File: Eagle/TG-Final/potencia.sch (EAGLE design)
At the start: 2 parts

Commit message: Schematic para Potencia
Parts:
- added D1: 15V, diode:ZENER-DIODEF126-10
- added IC1: 7812T, adafruit:7812T
- added JP2, JP3: (no value), SparkFun:M04LONGPADS
- added JP4: (no value), SparkFun:M06LONGPADS
- added LED1, LED2, LED3: (no value), adafruit:LED3MM
- added Q1: 2N3055, transistor-power:2N3055
- added R1, R3, R5: 1.8k, rcl:R-EU_0204/5
- added R10, R8, R9: 470, rcl:R-EU_0204/5
- added R11: 4.7K, rcl:R-EU_0204/5
- added R12: 1K, rcl:R-EU_0204/5
- added R2, R4, R6, R7: 1k, rcl:R-EU_0204/5
- added SG1: BUZZERPTH, SparkFun:BUZZERPTH
- added T1: 2N3904, transistor:2N3904
- added X1, X2, X3: (no value), con-wago-508:W237-2N
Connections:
- new net N$10: LED3.C, U$1.RB2/RX
- new net N$11: LED1.A, R8.2
- new net N$12: JP4.3, U$1.RB7/PGD
- new net N$13: LED2.A, R9.2
- new net N$14: LED3.A, R10.2
- new net N$15: JP4.2, U$1.RB6/PGC
- new net N$16: JP4.6, R7.2, U$1.RA5/MCLR
- new net N$17: R11.2, U$1.RB3
- new net N$18: X2-2.KL, X3-1.KL
- new net N$19: R11.1, T1.B
- new net N$2: R1.2, R2.1, U$1.RA0/AN0
- new net N$20: R12.1, SG1.1, T1.C
- new net N$21: D1.C, IC1.VI, X2-1.KL
- new net N$3: JP1.4, R3.1
- new net N$4: R3.2, R4.1, U$1.RA1/AN1
- new net N$5: JP2.4, R5.1
- new net N$6: R5.2, R6.1, U$1.RA2/AN2
- new net N$7: JP4.4, U$1.VSS
- new net N$8: LED1.C, U$1.RB0/INT
- new net N$9: LED2.C, U$1.RB1/SDA
- new net VDD: JP4.5, R10.1, R12.2, R7.1, R8.1, R9.1, SG1.2, U$1.VDD
- net N$1: now also JP3.4, R1.1; no longer JP1.2, U$1.RA4/AN4
- net VSS: now also D1.A, IC1.GND, JP2.1, JP3.1, R2.2, R4.2, R6.2, T1.E, X1-2.KL, X3-2.KL

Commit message: Esquematicos de Alimentación
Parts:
- added C1: 4700uf/25v, rcl:CPOL-USE10-30
- added C2, C3, C4: 0.1uf, rcl:C-EU050-024X044
- added C5: (no value), rcl:CPOL-USE2.5-6
- added D2: 1N4004, adafruit:1N4004
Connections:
- new net +12V: C4.1, C5.+, Q1.E
- new net N$22: C3.1, IC1.VO, Q1.B
- new net N$24: D2.A, IC1.GND
- net N$21: now also C1.+, C2.1, Q1.C
- net VSS: now also C1.-, C2.2, C3.2, C4.2, C5.-, D2.C; no longer IC1.GND
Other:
- moved on the sheet: D1, IC1, Q1
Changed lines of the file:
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@@
 <setting verticaltext="up"/>
 </settings>
-<grid distance="0.1" unitdist="inch" unit="inch" style="lines" multiple="1" display="no" altdistance="0.01" altunitdist="inch" altunit="inch"/>
+<grid distance="0.1" unitdist="inch" unit="inch" style="lines" multiple="1" display="yes" altdistance="0.01" altunitdist="inch" altunit="inch"/>
 <layers>
 <layer number="1" name="Top" color="4" fill="1" visible="no" active="no"/>
@@
 <part name="D1" library="diode" deviceset="ZENER-DIODE" device="F126-10" value="15V"/>
 <part name="VSS10" library="supply1" deviceset="VSS" device=""/>
+<part name="C1" library="rcl" deviceset="CPOL-US" device="E10-30" value="4700uf/25v"/>
+<part name="VSS12" library="supply1" deviceset="VSS" device=""/>
+<part name="C2" library="rcl" deviceset="C-EU" device="050-024X044" value="0.1uf"/>
 <part name="VSS11" library="supply1" deviceset="VSS" device=""/>
+<part name="D2" library="adafruit" deviceset="1N4004" device=""/>
+<part name="VSS13" library="supply1" deviceset="VSS" device=""/>
+<part name="C3" library="rcl" deviceset="C-EU" device="050-024X044" value="0.1uf"/>
+<part name="VSS14" library="supply1" deviceset="VSS" device=""/>
+<part name="C4" library="rcl" deviceset="C-EU" device="050-024X044" value="0.1uf"/>
+<part name="VSS15" library="supply1" deviceset="VSS" device=""/>
+<part name="C5" library="rcl" deviceset="CPOL-US" device="E2.5-6"/>
+<part name="VSS16" library="supply1" deviceset="VSS" device=""/>
+<part name="P+1" library="supply1" deviceset="+12V" device=""/>
 </parts>
 <sheets>
@@
 <instance part="X3" gate="-1" x="27.94" y="30.48"/>
 <instance part="X3" gate="-2" x="27.94" y="25.4"/>
-<instance part="VSS8" gate="G$1" x="35.56" y="20.32"/>
+<instance part="VSS8" gate="G$1" x="35.56" y="10.16"/>
 <instance part="VSS9" gate="G$1" x="35.56" y="66.04"/>
-<instance part="Q1" gate="A" x="116.84" y="35.56" rot="R90"/>
-<instance part="IC1" gate="A1" x="73.66" y="43.18"/>
-<instance part="D1" gate="G$1" x="53.34" y="38.1" rot="R90"/>
-<instance part="VSS10" gate="G$1" x="53.34" y="30.48"/>
-<instance part="VSS11" gate="G$1" x="73.66" y="30.48"/>
+<instance part="Q1" gate="A" x="99.06" y="40.64" rot="R90"/>
+<instance part="IC1" gate="A1" x="86.36" y="33.02"/>
+<instance part="D1" gate="G$1" x="71.12" y="27.94" rot="R90"/>
+<instance part="VSS10" gate="G$1" x="71.12" y="10.16"/>
+<instance part="C1" gate="G$1" x="45.72" y="33.02"/>
+<instance part="VSS12" gate="G$1" x="45.72" y="10.16"/>
+<instance part="C2" gate="G$1" x="60.96" y="25.4"/>
+<instance part="VSS11" gate="G$1" x="60.96" y="10.16"/>
+<instance part="D2" gate="1" x="86.36" y="20.32" rot="R270"/>
+<instance part="VSS13" gate="G$1" x="86.36" y="10.16"/>
+<instance part="C3" gate="G$1" x="99.06" y="25.4"/>
+<instance part="VSS14" gate="G$1" x="99.06" y="10.16"/>
+<instance part="C4" gate="G$1" x="111.76" y="25.4"/>
+<instance part="VSS15" gate="G$1" x="111.76" y="10.16"/>
+<instance part="C5" gate="G$1" x="121.92" y="33.02"/>
+<instance part="VSS16" gate="G$1" x="121.92" y="10.16"/>
+<instance part="P+1" gate="1" x="129.54" y="48.26"/>
 </instances>
 <busses>
@@
 <pinref part="VSS8" gate="G$1" pin="VSS"/>
 <wire x1="33.02" y1="25.4" x2="35.56" y2="25.4" width="0.1524" layer="91"/>
-<wire x1="35.56" y1="25.4" x2="35.56" y2="22.86" width="0.1524" layer="91"/>
+<wire x1="35.56" y1="25.4" x2="35.56" y2="12.7" width="0.1524" layer="91"/>
 </segment>
 <segment>
@@
 <pinref part="D1" gate="G$1" pin="A"/>
 <pinref part="VSS10" gate="G$1" pin="VSS"/>
-<wire x1="53.34" y1="35.56" x2="53.34" y2="33.02" width="0.1524" layer="91"/>
-</segment>
-<segment>
+<wire x1="71.12" y1="25.4" x2="71.12" y2="12.7" width="0.1524" layer="91"/>
+</segment>
+<segment>
+<pinref part="VSS12" gate="G$1" pin="VSS"/>
+<pinref part="C1" gate="G$1" pin="-"/>
+<wire x1="45.72" y1="12.7" x2="45.72" y2="27.94" width="0.1524" layer="91"/>
+</segment>
+<segment>
+<pinref part="VSS11" gate="G$1" pin="VSS"/>
+<pinref part="C2" gate="G$1" pin="2"/>
+<wire x1="60.96" y1="12.7" x2="60.96" y2="20.32" width="0.1524" layer="91"/>
+</segment>
+<segment>
+<pinref part="VSS13" gate="G$1" pin="VSS"/>
+<pinref part="D2" gate="1" pin="C"/>
+<wire x1="86.36" y1="12.7" x2="86.36" y2="17.78" width="0.1524" layer="91"/>
+</segment>
+<segment>
+<pinref part="VSS14" gate="G$1" pin="VSS"/>
+<pinref part="C3" gate="G$1" pin="2"/>
+<wire x1="99.06" y1="12.7" x2="99.06" y2="20.32" width="0.1524" layer="91"/>
+</segment>
+<segment>
+<pinref part="VSS15" gate="G$1" pin="VSS"/>
+<pinref part="C4" gate="G$1" pin="2"/>
+<wire x1="111.76" y1="12.7" x2="111.76" y2="20.32" width="0.1524" layer="91"/>
+</segment>
+<segment>
+<pinref part="C5" gate="G$1" pin="-"/>
+<pinref part="VSS16" gate="G$1" pin="VSS"/>
+<wire x1="121.92" y1="27.94" x2="121.92" y2="12.7" width="0.1524" layer="91"/>
+</segment>
+</net>
+<net name="N$21" class="0">
+<segment>
+<pinref part="X2" gate="-1" pin="KL"/>
+<wire x1="33.02" y1="43.18" x2="45.72" y2="43.18" width="0.1524" layer="91"/>
+<pinref part="C1" gate="G$1" pin="+"/>
+<wire x1="45.72" y1="35.56" x2="45.72" y2="43.18" width="0.1524" layer="91"/>
+<pinref part="Q1" gate="A" pin="C"/>
+<wire x1="93.98" y1="43.18" x2="60.96" y2="43.18" width="0.1524" layer="91"/>
+<pinref part="C2" gate="G$1" pin="1"/>
+<wire x1="60.96" y1="43.18" x2="45.72" y2="43.18" width="0.1524" layer="91"/>
+<wire x1="60.96" y1="27.94" x2="60.96" y2="33.02" width="0.1524" layer="91"/>
+<pinref part="IC1" gate="A1" pin="VI"/>
+<wire x1="60.96" y1="33.02" x2="60.96" y2="43.18" width="0.1524" layer="91"/>
+<wire x1="76.2" y1="33.02" x2="71.12" y2="33.02" width="0.1524" layer="91"/>
+<wire x1="71.12" y1="33.02" x2="60.96" y2="33.02" width="0.1524" layer="91"/>
+<pinref part="D1" gate="G$1" pin="C"/>
+<wire x1="71.12" y1="30.48" x2="71.12" y2="33.02" width="0.1524" layer="91"/>
+<junction x="71.12" y="33.02"/>
+<junction x="60.96" y="33.02"/>
+<junction x="60.96" y="43.18"/>
+<junction x="45.72" y="43.18"/>
+</segment>
+</net>
+<net name="N$22" class="0">
+<segment>
+<pinref part="IC1" gate="A1" pin="VO"/>
+<pinref part="Q1" gate="A" pin="B"/>
+<wire x1="96.52" y1="33.02" x2="99.06" y2="33.02" width="0.1524" layer="91"/>
+<wire x1="99.06" y1="33.02" x2="99.06" y2="38.1" width="0.1524" layer="91"/>
+<pinref part="C3" gate="G$1" pin="1"/>
+<wire x1="99.06" y1="27.94" x2="99.06" y2="33.02" width="0.1524" layer="91"/>
+<junction x="99.06" y="33.02"/>
+</segment>
+</net>
+<net name="N$24" class="0">
+<segment>
+<pinref part="D2" gate="1" pin="A"/>
 <pinref part="IC1" gate="A1" pin="GND"/>
-<pinref part="VSS11" gate="G$1" pin="VSS"/>
-<wire x1="73.66" y1="35.56" x2="73.66" y2="33.02" width="0.1524" layer="91"/>
-</segment>
-</net>
-<net name="N$21" class="0">
-<segment>
-<pinref part="IC1" gate="A1" pin="VI"/>
-<pinref part="D1" gate="G$1" pin="C"/>
-<wire x1="63.5" y1="43.18" x2="53.34" y2="43.18" width="0.1524" layer="91"/>
-<wire x1="53.34" y1="43.18" x2="53.34" y2="40.64" width="0.1524" layer="91"/>
-<pinref part="X2" gate="-1" pin="KL"/>
-<wire x1="33.02" y1="43.18" x2="53.34" y2="43.18" width="0.1524" layer="91"/>
-</segment>
-</net>
+<wire x1="86.36" y1="22.86" x2="86.36" y2="25.4" width="0.1524" layer="91"/>
+</segment>
+</net>
+<net name="+12V" class="0">
+<segment>
+<pinref part="P+1" gate="1" pin="+12V"/>
+<wire x1="129.54" y1="45.72" x2="129.54" y2="43.18" width="0.1524" layer="91"/>
+<pinref part="C4" gate="G$1" pin="1"/>
+<wire x1="111.76" y1="27.94" x2="111.76" y2="43.18" width="0.1524" layer="91"/>
+<pinref part="Q1" gate="A" pin="E"/>
+<wire x1="111.76" y1="43.18" x2="104.14" y2="43.18" width="0.1524" layer="91"/>
+<pinref part="C5" gate="G$1" pin="+"/>
+<wire x1="121.92" y1="35.56" x2="121.92" y2="43.18" width="0.1524" layer="91"/>
+<wire x1="121.92" y1="43.18" x2="111.76" y2="43.18" width="0.1524" layer="91"/>
+<wire x1="129.54" y1="43.18" x2="121.92" y2="43.18" width="0.1524" layer="91"/>
+<junction x="111.76" y="43.18"/>
+<junction x="121.92" y="43.18"/>
+</segment>
+</net>

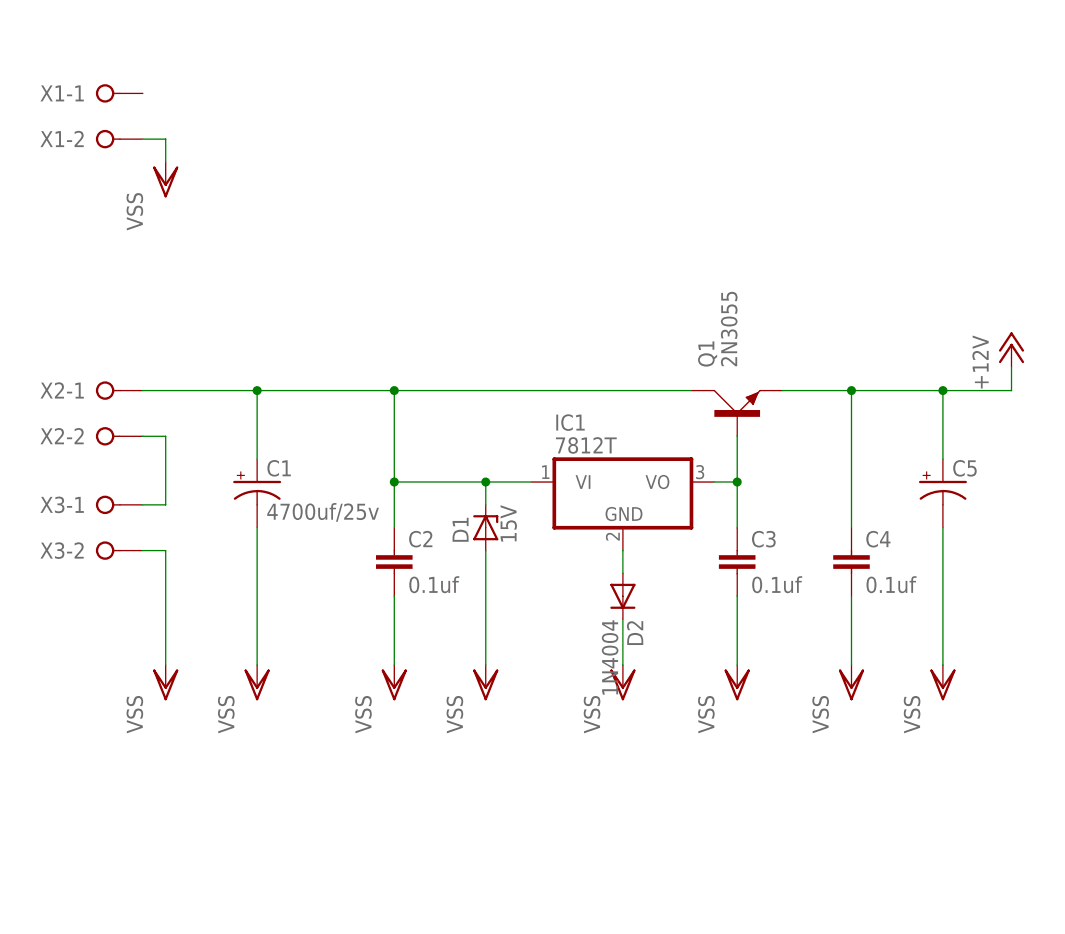
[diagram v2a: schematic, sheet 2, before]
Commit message: Esquematicos para placa logica
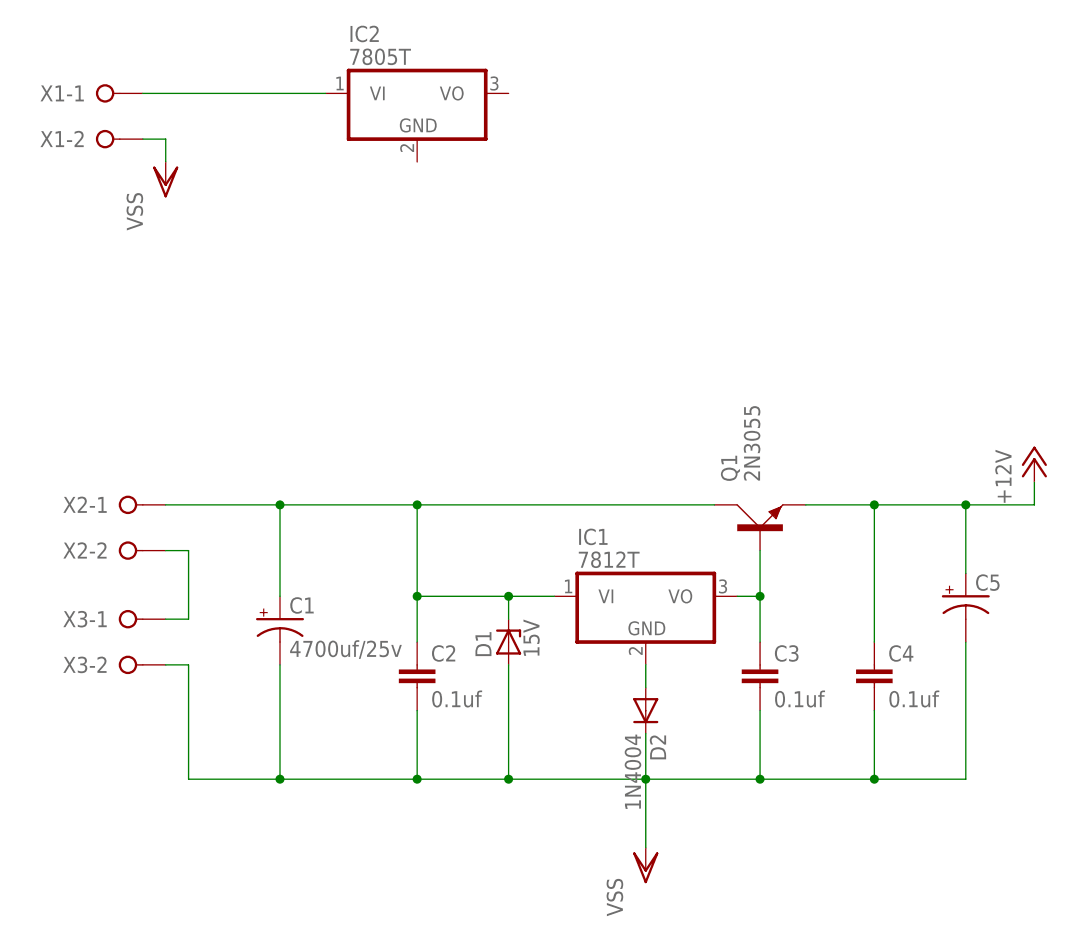
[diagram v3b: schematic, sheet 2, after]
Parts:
- added IC2: 7805T, adafruit:7805T
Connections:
- new net N$23: IC2.VI, X1-1.KL
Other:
- moved on the sheet: C1, C2, C3, C4, C5, D1, D2, IC1, Q1, X2-1, X2-2, X3-1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
